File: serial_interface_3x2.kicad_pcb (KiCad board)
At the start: 2 copper layers, 70.5 x 41.9 mm, 1 part

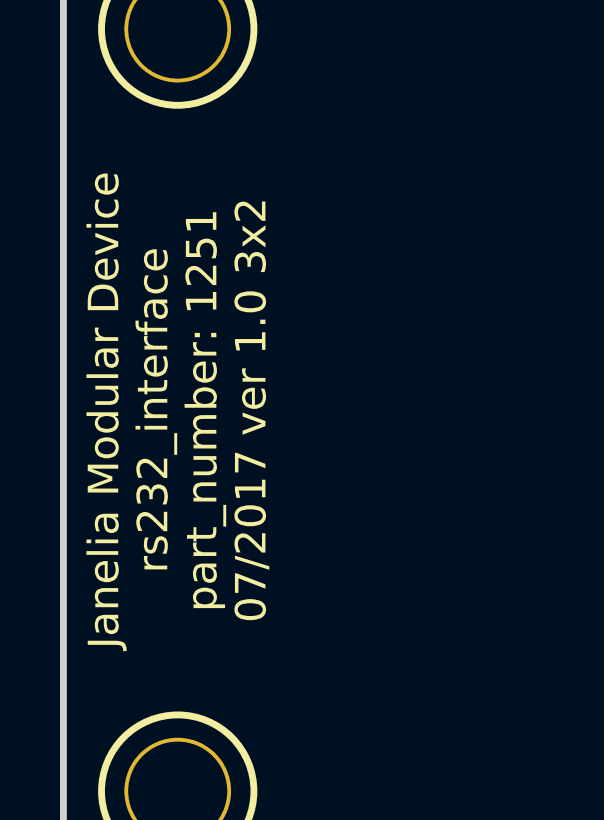
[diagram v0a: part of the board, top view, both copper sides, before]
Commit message: rs232 -> serial.
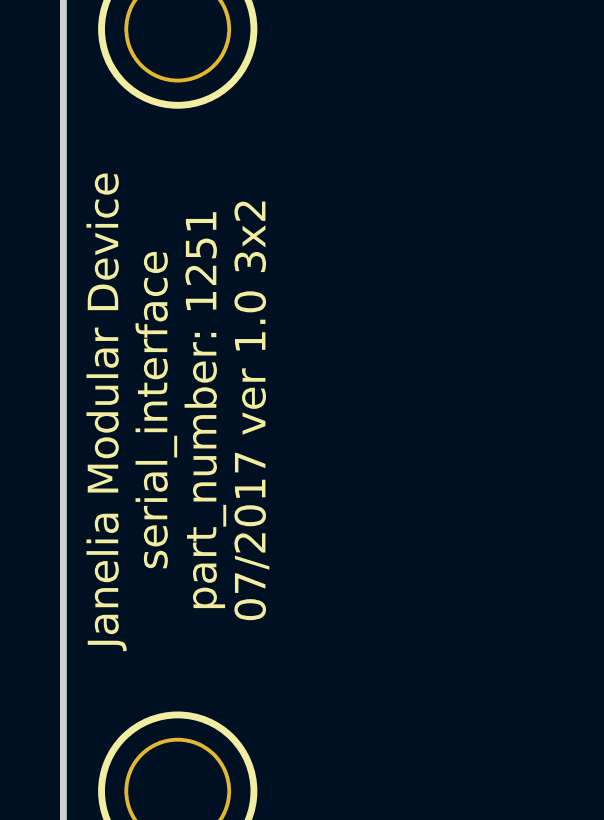
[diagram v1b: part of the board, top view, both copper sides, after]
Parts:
- MDB1: footprint rs232_interface_3x2:MODULAR_DEVICE_BASE_3X2_MALE -> serial_interface_3x2:MODULAR_DEVICE_BASE_3X2_MALE
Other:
- board text added: "Janelia Modular Device serial_interface part_number: 1251 07/2017 ver 1.0 3x2"
- board text removed: "Janelia Modular Device rs232_interface part_number: 1251 07/2017 ver 1.0 3x2"
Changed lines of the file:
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@@
   (page A4)
   (title_block
-    (title rs232_interface_3x2)
+    (title serial_interface_3x2)
     (rev 1.0)
   )
@@
     (diff_pair_width 0.254)
   )
-  (module rs232_interface_3x2:MODULAR_DEVICE_BASE_3X2_MALE (layer F.Cu)
+  (module serial_interface_3x2:MODULAR_DEVICE_BASE_3X2_MALE (layer F.Cu)
     (at 107.315 88.9)
     (fp_text reference MDB1 (at 0 0) (layer F.SilkS) hide
@@
     (effects (font (size 1.016 1.016) (thickness 0.1905)))
   )
-  (gr_text "Janelia Modular Device\nrs232_interface\npart_number: 1251\n07/2017 ver 1.0 3x2" (at 89.535 88.9 90) (layer F.SilkS)
+  (gr_text "Janelia Modular Device\nserial_interface\npart_number: 1251\n07/2017 ver 1.0 3x2" (at 89.535 88.9 90) (layer F.SilkS)
     (effects (font (size 1.016 1.016) (thickness 0.254)))
   )

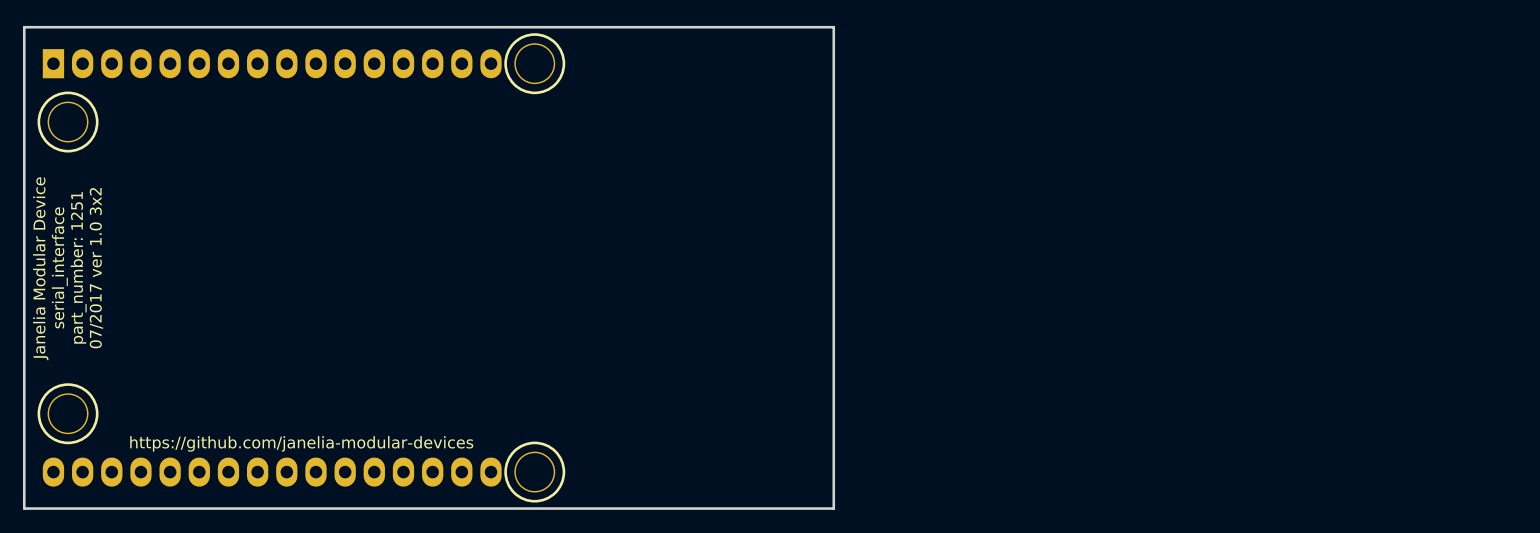
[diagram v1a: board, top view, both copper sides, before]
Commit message: Added RS232 components.
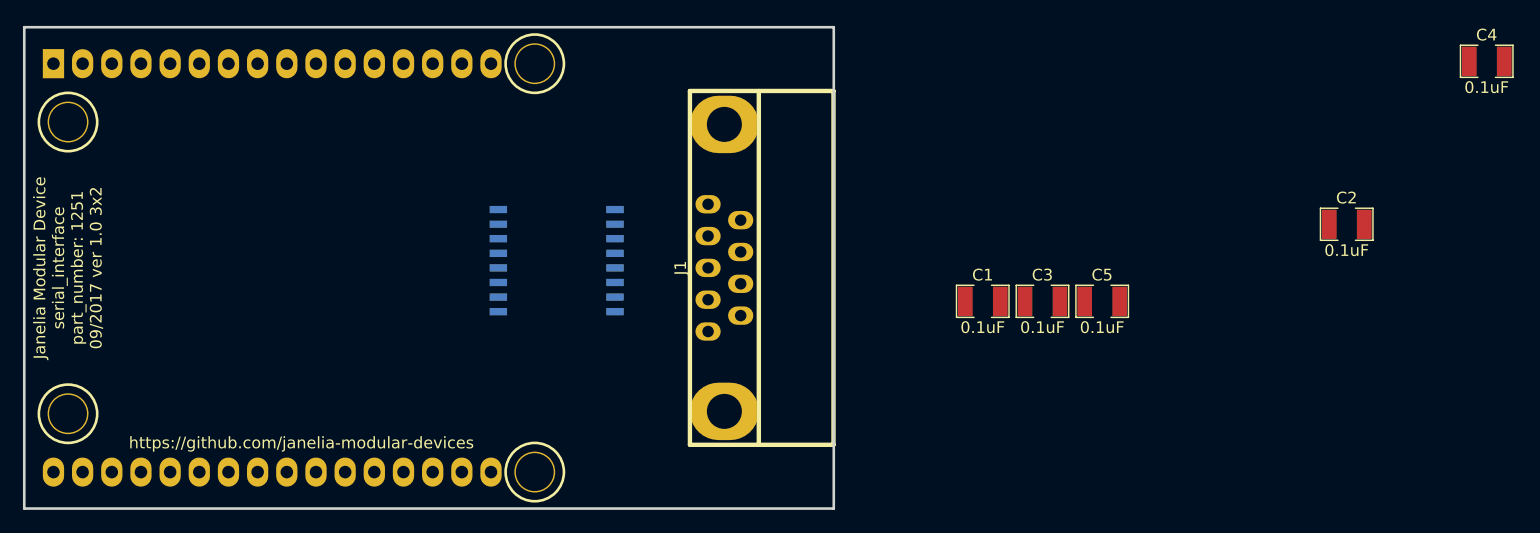
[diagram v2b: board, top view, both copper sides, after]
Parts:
- added C1: 0.1uF, serial_interface_3x2:SM1210, F.Cu at (169.2, 91.8)
- added C2: 0.1uF, serial_interface_3x2:SM1210, F.Cu at (200.9, 85.1)
- added C3: 0.1uF, serial_interface_3x2:SM1210, F.Cu at (174.4, 91.8)
- added C4: 0.1uF, serial_interface_3x2:SM1210, F.Cu at (213.1, 70.9)
- added C5: 0.1uF, serial_interface_3x2:SM1210, F.Cu at (179.6, 91.8)
- added J1: DB9M_RA, serial_interface_3x2:DB9M_RA, F.Cu at (146.7, 88.9)
- added U1: RS232_2x2, serial_interface_3x2:SOIC_16, B.Cu at (132.1, 88.9)
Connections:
- MDB1 pad 10: (no net) -> /TX2
- MDB1 pad 11: (no net) -> Net-(MDB1-Pad11)
- MDB1 pad 12: (no net) -> Net-(MDB1-Pad12)
- MDB1 pad 13: (no net) -> Net-(MDB1-Pad13)
- MDB1 pad 14: (no net) -> Net-(MDB1-Pad14)
- MDB1 pad 15: (no net) -> Net-(MDB1-Pad15)
- MDB1 pad 16: (no net) -> Net-(MDB1-Pad16)
- MDB1 pad 17: (no net) -> Net-(MDB1-Pad17)
- MDB1 pad 18: (no net) -> Net-(MDB1-Pad18)
- MDB1 pad 19: (no net) -> Net-(MDB1-Pad19)
- MDB1 pad 2: (no net) -> Net-(MDB1-Pad2)
- MDB1 pad 20: (no net) -> Net-(MDB1-Pad20)
- MDB1 pad 21: (no net) -> Net-(MDB1-Pad21)
- MDB1 pad 22: (no net) -> Net-(MDB1-Pad22)
- MDB1 pad 23: (no net) -> Net-(MDB1-Pad23)
- MDB1 pad 24: (no net) -> Net-(MDB1-Pad24)
- MDB1 pad 25: (no net) -> Net-(MDB1-Pad25)
- MDB1 pad 28: (no net) -> Net-(MDB1-Pad28)
- MDB1 pad 29: (no net) -> Net-(MDB1-Pad29)
- MDB1 pad 3: (no net) -> Net-(MDB1-Pad3)
- MDB1 pad 30: (no net) -> Net-(MDB1-Pad30)
- MDB1 pad 3V3: (no net) -> +3V3
- MDB1 pad 4: (no net) -> Net-(MDB1-Pad4)
- MDB1 pad 5: (no net) -> Net-(MDB1-Pad5)
- MDB1 pad 6: (no net) -> Net-(MDB1-Pad6)
- MDB1 pad 9: (no net) -> /RX2
- MDB1 pad AGND: (no net) -> Net-(MDB1-PadAGND)
- MDB1 pad AREF: (no net) -> Net-(MDB1-PadAREF)
- MDB1 pad DAC: (no net) -> Net-(MDB1-PadDAC)
- MDB1 pad GND: (no net) -> GND
- MDB1 pad VDD: (no net) -> VDD
- MDB1 pad VEE: (no net) -> VEE
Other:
- net class Default: trace_width 0.254 -> 0.25
- board text added: "Janelia Modular Device serial_interface part_number: 1251 09/2017 ver 1.0 3x2"
- board text removed: "Janelia Modular Device serial_interface part_number: 1251 07/2017 ver 1.0 3x2"

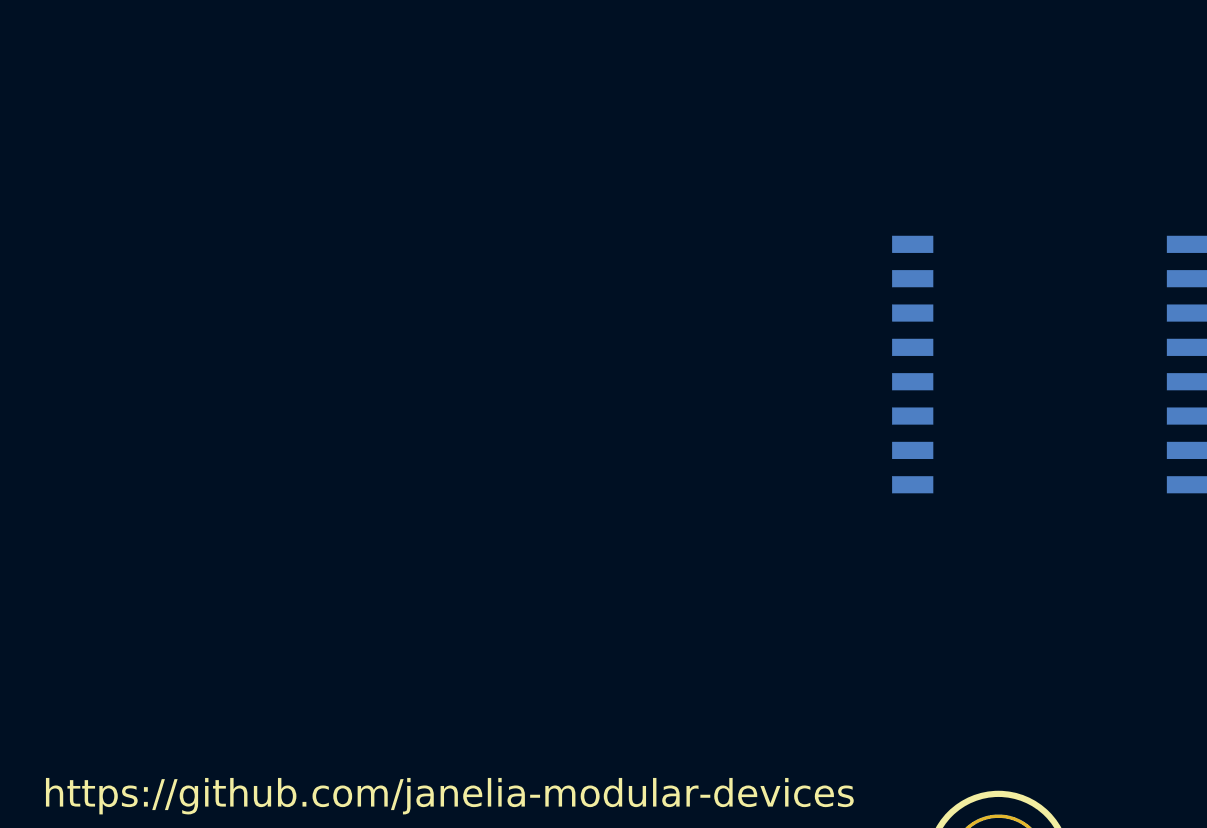
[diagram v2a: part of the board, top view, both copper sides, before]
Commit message: Added 2 port RJ45.
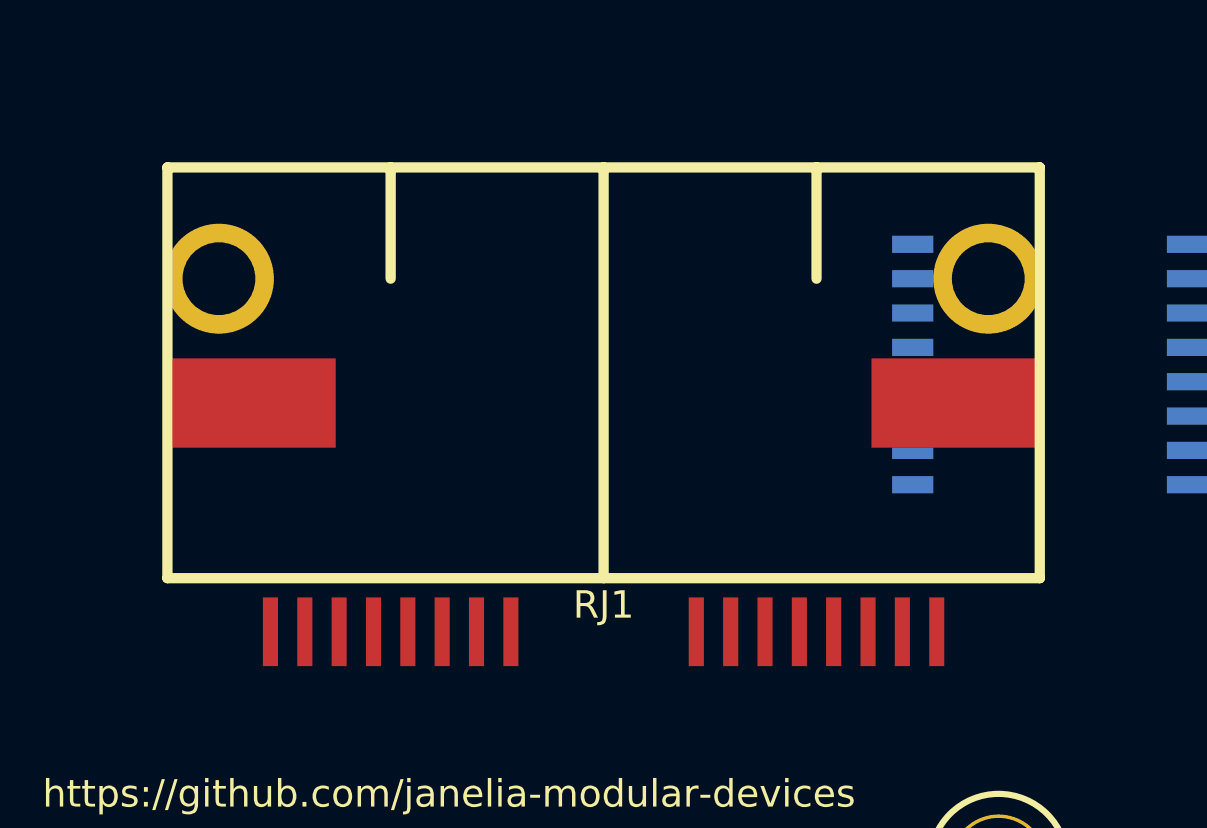
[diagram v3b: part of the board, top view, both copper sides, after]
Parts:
- added RJ1: RJ45_8P8C_2PORT_1ROW_RA_SMD, serial_interface_3x2:RJ45_8P8C_2PORT_1ROW_RA_SMD, F.Cu at (115.6, 85.1)
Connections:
- J1 pad 1: Net-(J1-Pad1) -> (no net)
- J1 pad 4: Net-(J1-Pad4) -> (no net)
- J1 pad 6: Net-(J1-Pad6) -> (no net)
- J1 pad 7: Net-(J1-Pad7) -> (no net)
- J1 pad 8: Net-(J1-Pad8) -> (no net)
- J1 pad 9: Net-(J1-Pad9) -> (no net)
- MDB1 pad 11: Net-(MDB1-Pad11) -> (no net)
- MDB1 pad 12: Net-(MDB1-Pad12) -> (no net)
- MDB1 pad 13: Net-(MDB1-Pad13) -> (no net)
- MDB1 pad 14: Net-(MDB1-Pad14) -> (no net)
- MDB1 pad 15: Net-(MDB1-Pad15) -> (no net)
- MDB1 pad 16: Net-(MDB1-Pad16) -> (no net)
- MDB1 pad 17: Net-(MDB1-Pad17) -> (no net)
- MDB1 pad 18: Net-(MDB1-Pad18) -> (no net)
- MDB1 pad 19: Net-(MDB1-Pad19) -> (no net)
- MDB1 pad 2: Net-(MDB1-Pad2) -> (no net)
- MDB1 pad 20: Net-(MDB1-Pad20) -> (no net)
- MDB1 pad 21: Net-(MDB1-Pad21) -> (no net)
- MDB1 pad 22: Net-(MDB1-Pad22) -> (no net)
- MDB1 pad 23: Net-(MDB1-Pad23) -> (no net)
- MDB1 pad 24: Net-(MDB1-Pad24) -> (no net)
- MDB1 pad 25: Net-(MDB1-Pad25) -> (no net)
- MDB1 pad 28: Net-(MDB1-Pad28) -> (no net)
- MDB1 pad 29: Net-(MDB1-Pad29) -> (no net)
- MDB1 pad 3: Net-(MDB1-Pad3) -> (no net)
- MDB1 pad 30: Net-(MDB1-Pad30) -> (no net)
- MDB1 pad 4: Net-(MDB1-Pad4) -> (no net)
- MDB1 pad 5: Net-(MDB1-Pad5) -> (no net)
- MDB1 pad 6: Net-(MDB1-Pad6) -> (no net)
- MDB1 pad AGND: Net-(MDB1-PadAGND) -> (no net)
- MDB1 pad AREF: Net-(MDB1-PadAREF) -> (no net)
- MDB1 pad DAC: Net-(MDB1-PadDAC) -> (no net)
- MDB1 pad VDD: VDD -> (no net)
- MDB1 pad VEE: VEE -> (no net)
